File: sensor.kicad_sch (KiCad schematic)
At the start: 5 parts, among them J7 sensor

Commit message: Re-linking the PCB properties back to the schematics
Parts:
- R11, R14, R15, R16: footprint Resistor_SMD:R_0201_0603Metric -> Library:R_0402_1005
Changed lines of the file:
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@@
 			)
 		)
-		(property "Footprint" "Resistor_SMD:R_0201_0603Metric"
+		(property "Footprint" "Library:R_0402_1005"
 			(at 78.74 60.96 0)
 			(effects
@@
 			)
 		)
-		(property "Footprint" "Resistor_SMD:R_0201_0603Metric"
+		(property "Footprint" "Library:R_0402_1005"
 			(at 78.74 68.58 0)
 			(effects
@@
 			)
 		)
-		(property "Footprint" "Resistor_SMD:R_0201_0603Metric"
+		(property "Footprint" "Library:R_0402_1005"
 			(at 78.74 63.5 0)
 			(effects
@@
 			)
 		)
-		(property "Footprint" "Resistor_SMD:R_0201_0603Metric"
+		(property "Footprint" "Library:R_0402_1005"
 			(at 78.74 66.04 0)
 			(effects

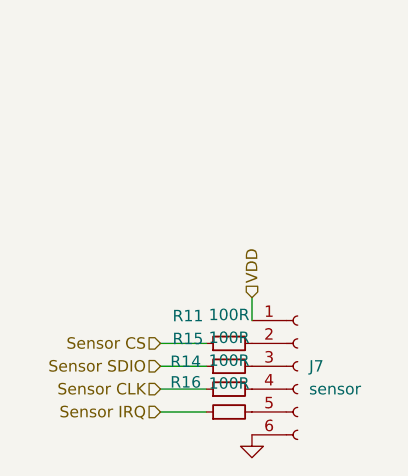
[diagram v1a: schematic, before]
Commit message: Sorting out most of the powerlines
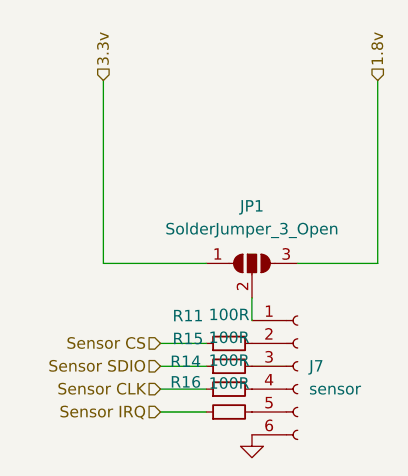
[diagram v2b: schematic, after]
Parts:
- added JP1: SolderJumper_3_Open, Jumper:SolderJumper-3_P1.3mm_Open_RoundedPad1.0x1.5mm, symbol Jumper:SolderJumper_3_Open
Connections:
- net VDD: no longer names the net of J7.1 (Pin_1)
- net VDD: now also JP1.2 (C)
- new net 1.8v: JP1.3 (B)
- new net 3.3v: JP1.1 (A)
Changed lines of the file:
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@@
+	(wire
+		(pts
+			(xy 64.77 31.75) (xy 64.77 52.07)
+		)
+		(stroke
+			(width 0)
+			(type default)
+		)
+	)
+	(wire
+		(pts
+			(xy 95.25 31.75) (xy 95.25 52.07)
+		)
+		(stroke
+			(width 0)
+			(type default)
+		)
+	)
 	(wire
 		(pts
 			(xy 81.28 55.88) (xy 81.28 58.42)
+		)
+		(stroke
+			(width 0)
+			(type default)
+		)
+	)
+	(wire
+		(pts
+			(xy 95.25 52.07) (xy 86.36 52.07)
+		)
+		(stroke
+			(width 0)
+			(type default)
+		)
+	)
+	(wire
+		(pts
+			(xy 64.77 52.07) (xy 76.2 52.07)
 		)
 		(stroke
@@
 		)
 	)
-	(hierarchical_label "VDD"
+	(hierarchical_label "1.8v"
 		(shape input)
-		(at 81.28 55.88 90)
+		(at 95.25 31.75 90)
+		(effects
+			(font
+				(size 1.27 1.27)
+			)
+			(justify left)
+		)
+	)
+	(hierarchical_label "3.3v"
+		(shape input)
+		(at 64.77 31.75 90)
 		(effects
 			(font
@@
 		)
 	)
+	(symbol
+		(lib_id "Jumper:SolderJumper_3_Open")
+		(at 81.28 52.07 0)
+		(unit 1)
+		(exclude_from_sim no)
+		(in_bom no)
+		(on_board yes)
+		(dnp no)
+		(fields_autoplaced yes)
+		(property "Reference" "JP1"
+			(at 81.28 45.72 0)
+			(effects
+				(font
+					(size 1.27 1.27)
+				)
+			)
+		)
+		(property "Value" "SolderJumper_3_Open"
+			(at 81.28 48.26 0)
+			(effects
+				(font
+					(size 1.27 1.27)
+				)
+			)
+		)
+		(property "Footprint" "Jumper:SolderJumper-3_P1.3mm_Open_RoundedPad1.0x1.5mm"
+			(at 81.28 52.07 0)
+			(effects
+				(font
+					(size 1.27 1.27)
+				)
+				(hide yes)
+			)
+		)
+		(property "Datasheet" "~"
+			(at 81.28 52.07 0)
+			(effects
+				(font
+					(size 1.27 1.27)
+				)
+				(hide yes)
+			)
+		)
+		(property "Description" "Solder Jumper, 3-pole, open"
+			(at 81.28 52.07 0)
+			(effects
+				(font
+					(size 1.27 1.27)
+				)
+				(hide yes)
+			)
+		)
+		(pin "1"
+		)
+		(pin "3"
+		)
+		(pin "2"
+		)
+		(instances
+			(project ""
+				(path "/3a835e6f-a660-4b38-a102-87841cdd95ed/ad95ea7c-7575-44c2-8b98-616af50ac5d2"
+					(reference "JP1")
+					(unit 1)
+				)
+			)
+		)
+	)

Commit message: Further optimising the BOM and adding JLCPCB specific part numbers
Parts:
- J7: LCSC (none) -> C160405
- R11, R14, R15, R16: LCSC (none) -> C25076
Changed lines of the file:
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@@
+			)
+		)
+		(property "AVAILABILITY" ""
+			(at 81.28 52.07 0)
+			(effects
+				(font
+					(size 1.27 1.27)
+				)
+				(hide yes)
+			)
+		)
+		(property "DESCRIPTION" ""
+			(at 81.28 52.07 0)
+			(effects
+				(font
+					(size 1.27 1.27)
+				)
+				(hide yes)
+			)
+		)
+		(property "PACKAGE" ""
+			(at 81.28 52.07 0)
+			(effects
+				(font
+					(size 1.27 1.27)
+				)
+				(hide yes)
+			)
+		)
+		(property "PRICE" ""
+			(at 81.28 52.07 0)
+			(effects
+				(font
+					(size 1.27 1.27)
+				)
+				(hide yes)
 			)
 		)
@@
 			)
 		)
-		(property "LCSC" ""
+		(property "LCSC" "C25076"
 			(at 78.74 60.96 0)
+			(effects
+				(font
+					(size 1.27 1.27)
+				)
+				(hide yes)
+			)
+		)
+		(property "AVAILABILITY" ""
+			(at 78.74 60.96 90)
+			(effects
+				(font
+					(size 1.27 1.27)
+				)
+				(hide yes)
+			)
+		)
+		(property "DESCRIPTION" ""
+			(at 78.74 60.96 90)
+			(effects
+				(font
+					(size 1.27 1.27)
+				)
+				(hide yes)
+			)
+		)
+		(property "PACKAGE" ""
+			(at 78.74 60.96 90)
+			(effects
+				(font
+					(size 1.27 1.27)
+				)
+				(hide yes)
+			)
+		)
+		(property "PRICE" ""
+			(at 78.74 60.96 90)
 			(effects
 				(font
@@
 			)
 		)
-		(property "LCSC" ""
+		(property "LCSC" "C25076"
 			(at 78.74 68.58 0)
+			(effects
+				(font
+					(size 1.27 1.27)
+				)
+				(hide yes)
+			)
+		)
+		(property "AVAILABILITY" ""
+			(at 78.74 68.58 90)
+			(effects
+				(font
+					(size 1.27 1.27)
+				)
+				(hide yes)
+			)
+		)
+		(property "DESCRIPTION" ""
+			(at 78.74 68.58 90)
+			(effects
+				(font
+					(size 1.27 1.27)
+				)
+				(hide yes)
+			)
+		)
+		(property "PACKAGE" ""
+			(at 78.74 68.58 90)
+			(effects
+				(font
+					(size 1.27 1.27)
+				)
+				(hide yes)
+			)
+		)
+		(property "PRICE" ""
+			(at 78.74 68.58 90)
 			(effects
 				(font
@@
 			)
 		)
+		(property "AVAILABILITY" ""
+			(at 86.36 63.5 0)
+			(effects
+				(font
+					(size 1.27 1.27)
+				)
+				(hide yes)
+			)
+		)
+		(property "DESCRIPTION" ""
+			(at 86.36 63.5 0)
+			(effects
+				(font
+					(size 1.27 1.27)
+				)
+				(hide yes)
+			)
+		)
+		(property "PACKAGE" ""
+			(at 86.36 63.5 0)
+			(effects
+				(font
+					(size 1.27 1.27)
+				)
+				(hide yes)
+			)
+		)
+		(property "PRICE" ""
+			(at 86.36 63.5 0)
+			(effects
+				(font
+					(size 1.27 1.27)
+				)
+				(hide yes)
+			)
+		)
+		(property "LCSC" "C160405"
+			(at 86.36 63.5 0)
+			(effects
+				(font
+					(size 1.27 1.27)
+				)
+				(hide yes)
+			)
+		)
 		(pin "1"
 		)
@@
 			)
 		)
-		(property "LCSC" ""
+		(property "LCSC" "C25076"
 			(at 78.74 63.5 0)
+			(effects
+				(font
+					(size 1.27 1.27)
+				)
+				(hide yes)
+			)
+		)
+		(property "AVAILABILITY" ""
+			(at 78.74 63.5 90)
+			(effects
+				(font
+					(size 1.27 1.27)
+				)
+				(hide yes)
+			)
+		)
+		(property "DESCRIPTION" ""
+			(at 78.74 63.5 90)
+			(effects
+				(font
+					(size 1.27 1.27)
+				)
+				(hide yes)
+			)
+		)
+		(property "PACKAGE" ""
+			(at 78.74 63.5 90)
+			(effects
+				(font
+					(size 1.27 1.27)
+				)
+				(hide yes)
+			)
+		)
+		(property "PRICE" ""
+			(at 78.74 63.5 90)
 			(effects
 				(font
@@
 			)
 		)
-		(property "LCSC" ""
+		(property "LCSC" "C25076"
 			(at 78.74 66.04 0)
 			(effects
 				(font
+					(size 1.27 1.27)
+				)
+				(hide yes)
+			)
+		)
+		(property "AVAILABILITY" ""
+			(at 78.74 66.04 90)
+			(effects
+				(font
+					(size 1.27 1.27)
+				)
+				(hide yes)
+			)
+		)
+		(property "DESCRIPTION" ""
+			(at 78.74 66.04 90)
+			(effects
+				(font
+					(size 1.27 1.27)
+				)
+				(hide yes)
+			)
+		)
+		(property "PACKAGE" ""
+			(at 78.74 66.04 90)
+			(effects
+				(font
+					(size 1.27 1.27)
+				)
+				(hide yes)
+			)
+		)
+		(property "PRICE" ""
+			(at 78.74 66.04 90)
+			(effects
+				(font

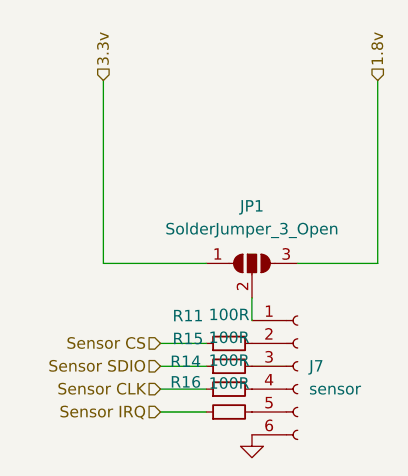
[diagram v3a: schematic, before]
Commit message: Removing the 1.8v power supply option
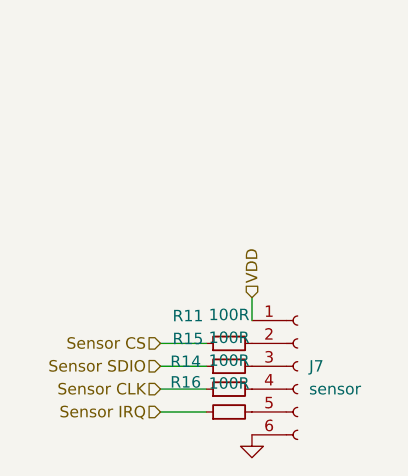
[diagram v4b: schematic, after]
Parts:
- removed JP1: SolderJumper_3_Open, Jumper:SolderJumper-3_P1.3mm_Open_RoundedPad1.0x1.5mm, symbol Jumper:SolderJumper_3_Open
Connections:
- net VDD: now reaches J7.1 (Pin_1)
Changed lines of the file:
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@@
-	(wire
-		(pts
-			(xy 64.77 31.75) (xy 64.77 52.07)
-		)
-		(stroke
-			(width 0)
-			(type default)
-		)
-	)
-	(wire
-		(pts
-			(xy 95.25 31.75) (xy 95.25 52.07)
-		)
-		(stroke
-			(width 0)
-			(type default)
-		)
-	)
 	(wire
 		(pts
 			(xy 81.28 55.88) (xy 81.28 58.42)
-		)
-		(stroke
-			(width 0)
-			(type default)
-		)
-	)
-	(wire
-		(pts
-			(xy 95.25 52.07) (xy 86.36 52.07)
-		)
-		(stroke
-			(width 0)
-			(type default)
-		)
-	)
-	(wire
-		(pts
-			(xy 64.77 52.07) (xy 76.2 52.07)
 		)
 		(stroke
@@
 		)
 	)
-	(hierarchical_label "1.8v"
-		(shape input)
-		(at 95.25 31.75 90)
-		(effects
-			(font
-				(size 1.27 1.27)
-			)
-			(justify left)
-		)
-	)
-	(hierarchical_label "3.3v"
-		(shape input)
-		(at 64.77 31.75 90)
-		(effects
-			(font
-				(size 1.27 1.27)
-			)
-			(justify left)
-		)
-	)
 	(hierarchical_label "Sensor SDIO"
 		(shape input)
@@
 		)
 	)
+	(hierarchical_label "VDD"
+		(shape input)
+		(at 81.28 55.88 90)
+		(effects
+			(font
+				(size 1.27 1.27)
+			)
+			(justify left)
+		)
+	)
 	(hierarchical_label "Sensor CS"
 		(shape input)
@@
 		)
 	)
-	(symbol
-		(lib_id "Jumper:SolderJumper_3_Open")
-		(at 81.28 52.07 0)
-		(unit 1)
-		(exclude_from_sim no)
-		(in_bom no)
-		(on_board yes)
-		(dnp no)
-		(fields_autoplaced yes)
-		(property "Reference" "JP1"
-			(at 81.28 45.72 0)
-			(effects
-				(font
-					(size 1.27 1.27)
-				)
-			)
-		)
-		(property "Value" "SolderJumper_3_Open"
-			(at 81.28 48.26 0)
-			(effects
-				(font
-					(size 1.27 1.27)
-				)
-			)
-		)
-		(property "Footprint" "Jumper:SolderJumper-3_P1.3mm_Open_RoundedPad1.0x1.5mm"
-			(at 81.28 52.07 0)
-			(effects
-				(font
-					(size 1.27 1.27)
-				)
-				(hide yes)
-			)
-		)
-		(property "Datasheet" "~"
-			(at 81.28 52.07 0)
-			(effects
-				(font
-					(size 1.27 1.27)
-				)
-				(hide yes)
-			)
-		)
-		(property "Description" "Solder Jumper, 3-pole, open"
-			(at 81.28 52.07 0)
-			(effects
-				(font
-					(size 1.27 1.27)
-				)
-				(hide yes)
-			)
-		)
-		(property "AVAILABILITY" ""
-			(at 81.28 52.07 0)
-			(effects
-				(font
-					(size 1.27 1.27)
-				)
-				(hide yes)
-			)
-		)
-		(property "DESCRIPTION" ""
-			(at 81.28 52.07 0)
-			(effects
-				(font
-					(size 1.27 1.27)
-				)
-				(hide yes)
-			)
-		)
-		(property "PACKAGE" ""
-			(at 81.28 52.07 0)
-			(effects
-				(font
-					(size 1.27 1.27)
-				)
-				(hide yes)
-			)
-		)
-		(property "PRICE" ""
-			(at 81.28 52.07 0)
-			(effects
-				(font
-					(size 1.27 1.27)
-				)
-				(hide yes)
-			)
-		)
-		(pin "1"
-		)
-		(pin "3"
-		)
-		(pin "2"
-		)
-		(instances
-			(project ""
-				(path "/3a835e6f-a660-4b38-a102-87841cdd95ed/ad95ea7c-7575-44c2-8b98-616af50ac5d2"
-					(reference "JP1")
-					(unit 1)
-				)
-			)
-		)
-	)
